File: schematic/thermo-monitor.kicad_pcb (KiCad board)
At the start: 2 copper layers, 26 x 49 mm, 12 parts, among them J1 Screw_Terminal_01x03, J2 Screw_Terminal_01x03, J3 Screw_Terminal_01x03, J4 Screw_Terminal_01x03, J5 Screw_Terminal_01x03, U8 TFT_320x240

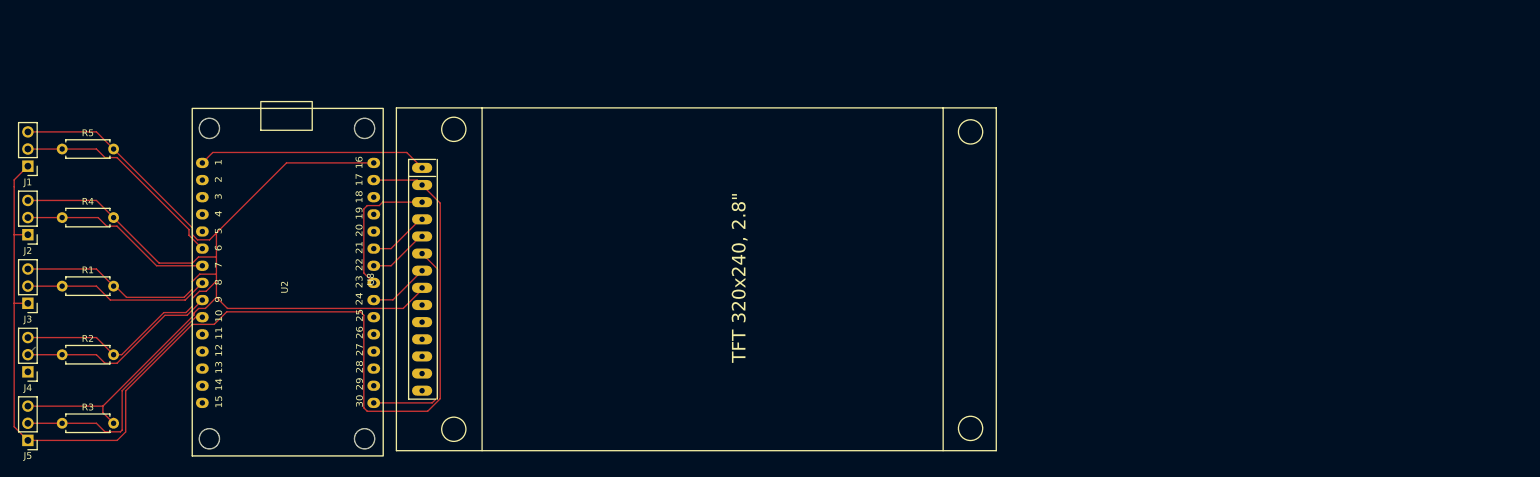
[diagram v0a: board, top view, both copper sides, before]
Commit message: feat: jack connectors && 5v dc port
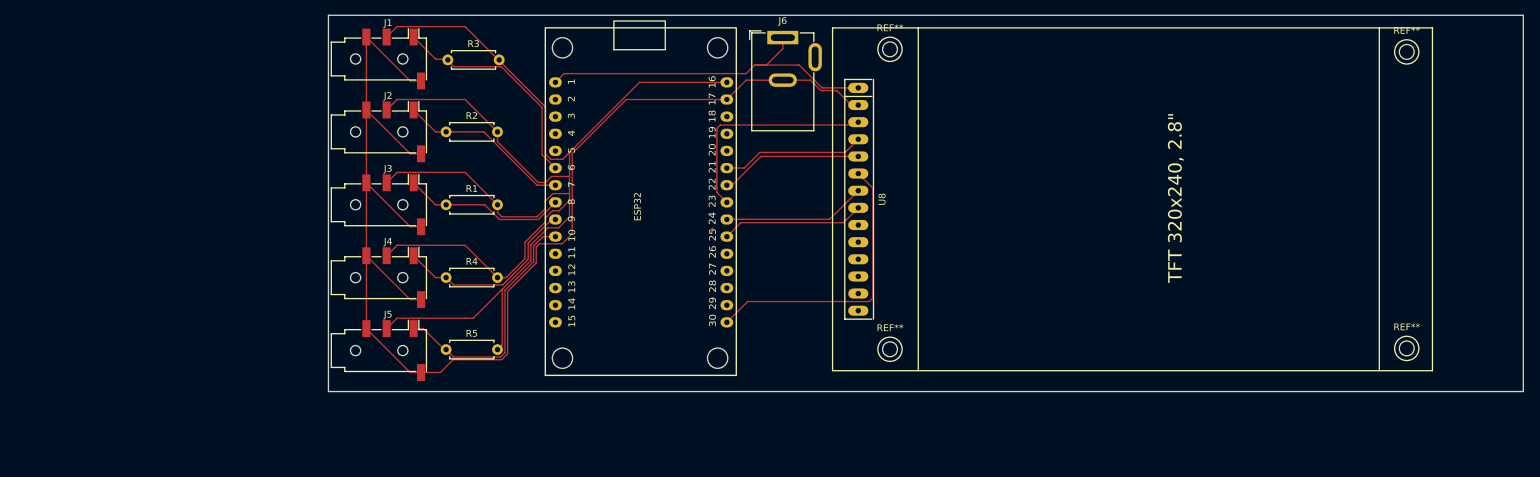
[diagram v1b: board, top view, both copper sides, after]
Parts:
- added J6: Barrel_Jack_Switch, Connector_BarrelJack:BarrelJack_GCT_DCJ200-10-A_Horizontal, F.Cu at (139.8, 82.5)
- added REF**: MountingHole_2.2mm_M2, MountingHole:MountingHole_2.2mm_M2, F.Cu at (155.7, 84.3)
- added REF**: MountingHole_2.2mm_M2, MountingHole:MountingHole_2.2mm_M2, F.Cu at (232.3, 84.7)
- added REF**: MountingHole_2.2mm_M2, MountingHole:MountingHole_2.2mm_M2, F.Cu at (155.7, 128.7)
- added REF**: MountingHole_2.2mm_M2, MountingHole:MountingHole_2.2mm_M2, F.Cu at (232.3, 128.6)
- J1, J2, J3, J4, J5: value Screw_Terminal_01x03 -> AudioJack4; footprint Connector_PinHeader_2.54mm:PinHeader_1x03_P2.54mm_Vertical -> Connector_Audio:Jack_3.5mm_PJ320D_Horizontal
- moved R3 78.5 mm to (90.2, 85.9)
- moved R2 65.8 mm to (89.9, 96.5)
- moved U8 65.7 mm to (151.0, 106.5)
- moved R5 64.2 mm to (89.9, 128.8)
- moved R1 58.2 mm to (89.9, 107.3)
- moved R4 57.6 mm to (89.9, 118.1)
- moved J1 55.7 mm to (81.3, 85.7), turned to 0 degrees
- moved J2 55.5 mm to (81.3, 96.5), turned to 0 degrees
- moved J3 55.3 mm to (81.3, 107.3), turned to 0 degrees
- moved J4 55.1 mm to (81.3, 118.1), turned to 0 degrees
- moved J5 55.0 mm to (81.3, 128.9), turned to 0 degrees
- moved ESP32 53.7 mm to (118.6, 107.2)
- renumbered U2 to ESP32
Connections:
- ESP32 pad 25: unconnected-(U2-GPIO19-Pad25) -> GPIO19
- R2 pad 1: GPIO33 -> GPIO26
- R3 pad 1: GPIO32 -> GPIO27
- R4 pad 1: GPIO26 -> GPIO33
- R5 pad 1: GPIO27 -> GPIO32
- U8 pad 8: +3V3 -> GPIO19
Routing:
- net GND: track 174.3 -> 196.0 mm
- net GPIO19: track 0.00 -> 21.2 mm
- net +5V: track 34.2 -> 54.2 mm
- net +3V3: track 241.9 -> 226.5 mm
- net GPIO17: track 8.97 -> 21.2 mm
- net GPIO16: track 9.21 -> 21.5 mm
- net SCK: track 8.97 -> 21.2 mm
- net CS: track 20.6 -> 32.9 mm
- net SDO: track 32.1 -> 42.5 mm
- net GPIO33: track 31.8 -> 28.3 mm
- net GPIO25: track 27.8 -> 24.3 mm
- net GPIO26: track 28.8 -> 25.6 mm
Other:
- board size 26 x 49 mm -> 177.1 x 55.8 mm

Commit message: feat: buttons on schematic
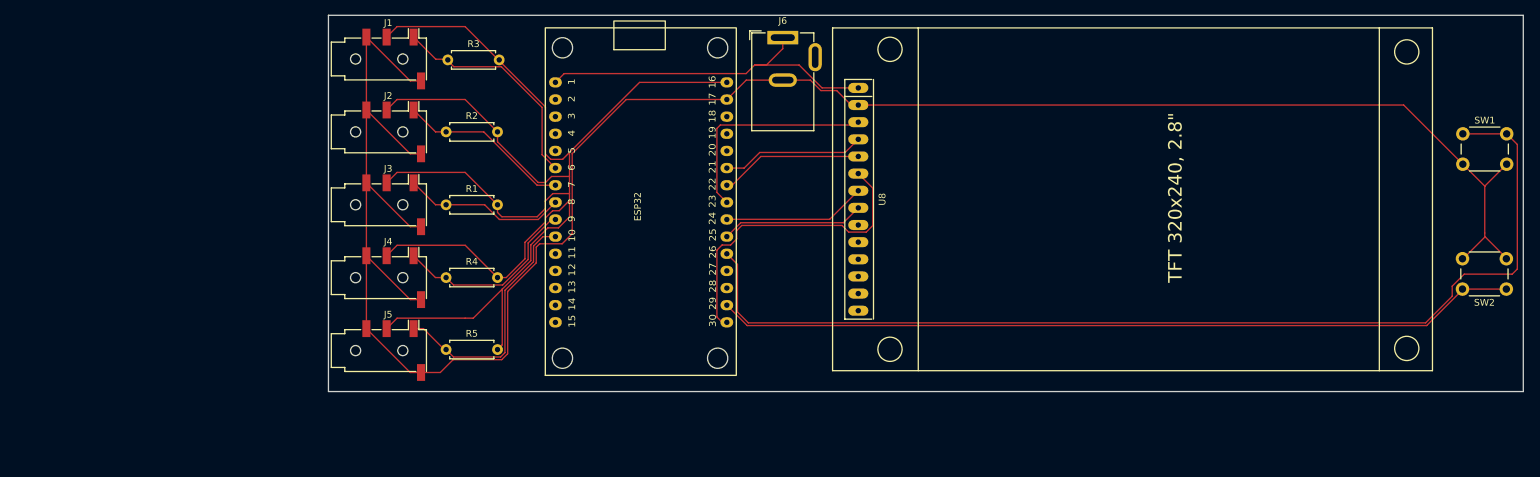
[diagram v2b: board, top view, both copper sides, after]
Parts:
- removed REF** (x4): MountingHole_2.2mm_M2, MountingHole:MountingHole_2.2mm_M2
- added SW1: SW_Push_Dual_x2, Button_Switch_THT:SW_PUSH_6mm_H13mm, F.Cu at (240.6, 96.8)
- added SW2: SW_Push_Dual_x2, Button_Switch_THT:SW_PUSH_6mm_H13mm, F.Cu at (247.0, 119.8)
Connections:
- ESP32 pad 26: unconnected-(ESP32-GPIO21-Pad26) -> GPIO21
- ESP32 pad 29: unconnected-(ESP32-GPIO22-Pad29) -> GPIO22
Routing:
- net GPIO21: track 0.00 -> 156.9 mm
- net GPIO22: track 0.00 -> 119.1 mm
- net GND: track 196.0 -> 314.5 mm
- net SDO: track 42.5 -> 46.5 mm

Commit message: feat: split to hpp and cpp
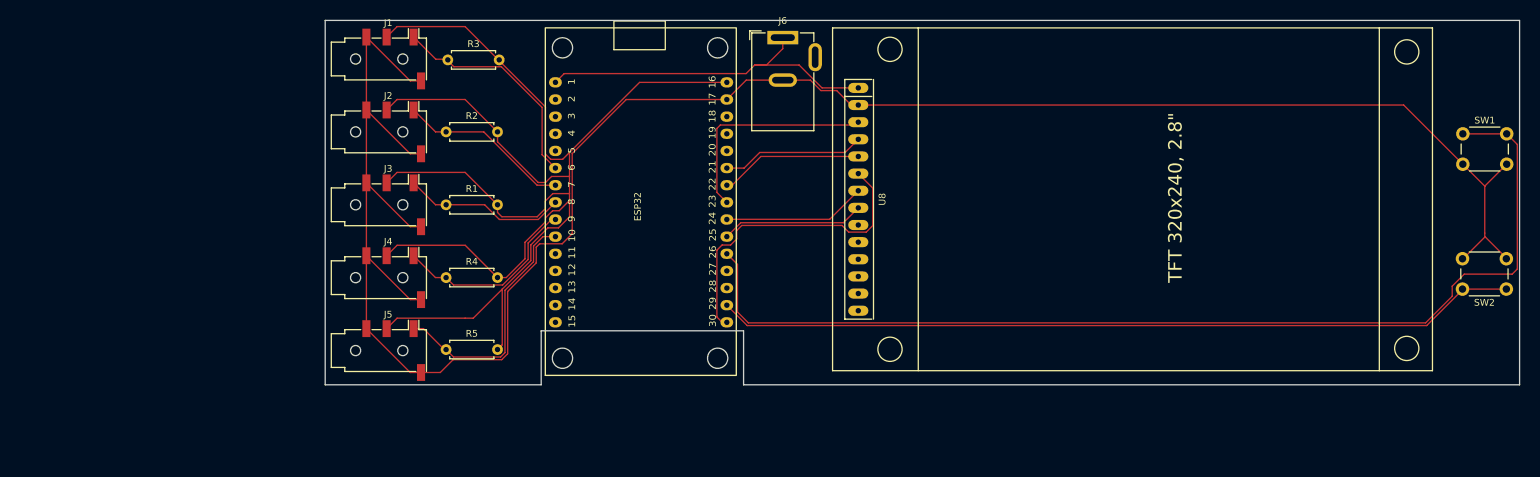
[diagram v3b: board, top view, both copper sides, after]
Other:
- board size 177.1 x 55.8 mm -> 177 x 54 mm
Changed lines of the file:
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@@
 		)
 	)
-	(gr_rect
-		(start 72.4804 79.2418)
-		(end 249.5534 135)
+	(gr_poly
+		(pts
+			(xy 104 126) (xy 134 126) (xy 134 134) (xy 249 134) (xy 249 80) (xy 72 80) (xy 72 134) (xy 104 134)
+		)
 		(stroke
 			(width 0.05)
-			(type default)
+			(type solid)
 		)
 		(fill no)

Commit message: fix psu 5v barell rotation
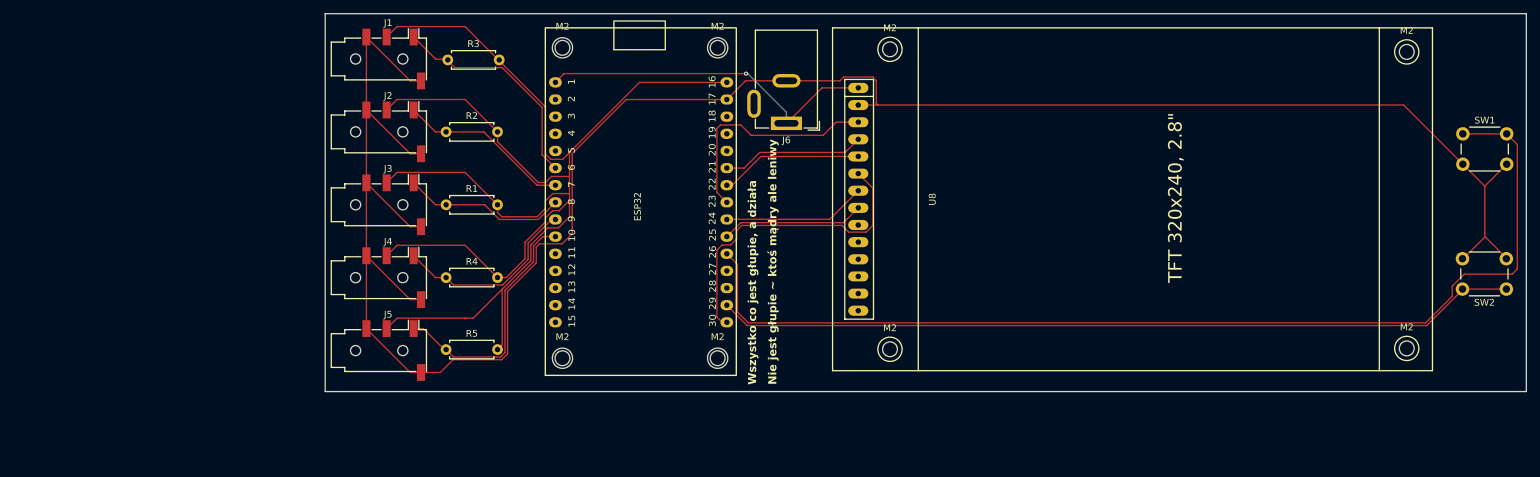
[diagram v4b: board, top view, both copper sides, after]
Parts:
- added M2: MountingHole_2.2mm_M2, MountingHole:MountingHole_2.2mm_M2, F.Cu at (155.7, 128.7)
- added M2: MountingHole_2.2mm_M2, MountingHole:MountingHole_2.2mm_M2, F.Cu at (232.3, 84.7)
- added M2: MountingHole_2.2mm_M2, MountingHole:MountingHole_2.2mm_M2, F.Cu at (130.2, 130.1)
- added M2: MountingHole_2.2mm_M2, MountingHole:MountingHole_2.2mm_M2, F.Cu at (232.3, 128.6)
- added M2: MountingHole_2.2mm_M2, MountingHole:MountingHole_2.2mm_M2, F.Cu at (107.2, 130.1)
- added M2: MountingHole_2.2mm_M2, MountingHole:MountingHole_2.2mm_M2, F.Cu at (130.2, 84.1)
- added M2: MountingHole_2.2mm_M2, MountingHole:MountingHole_2.2mm_M2, F.Cu at (155.7, 84.3)
- added M2: MountingHole_2.2mm_M2, MountingHole:MountingHole_2.2mm_M2, F.Cu at (107.2, 84.1)
- moved J6 12.7 mm to (140.3, 95.2), turned to 180 degrees
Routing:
- net GND: track 314.5 -> 320.9 mm
- net +5V: track 54.2 -> 51.6 mm, vias 0 -> 1
- net CS: track 32.9 -> 34.8 mm
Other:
- board size 177 x 54 mm -> 178 x 56 mm
- board text added: "Nie jest głupie ~ ktoś mądry ale leniwy"
- board text added: "Wszystko co jest głupie, a działa"
